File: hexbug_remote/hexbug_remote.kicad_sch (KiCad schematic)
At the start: 34 parts, among them J1 USB_C_Receptacle_USB2.0_16P, J2 Conn_01x02, J3 Conn_01x06, SW1 SW_Push, SW2 SW_Push, SW3 SW_Push, SW4 SW_Push, SW5 SW_Push, SW6 SW_Push, SW7 SW_SP4T_6PIN, SW8 SW_SPDT_3PIN, U1 TLV70033_SOT23-5, U2 MSPM01304xDGS20, U3 BQ21040DBV

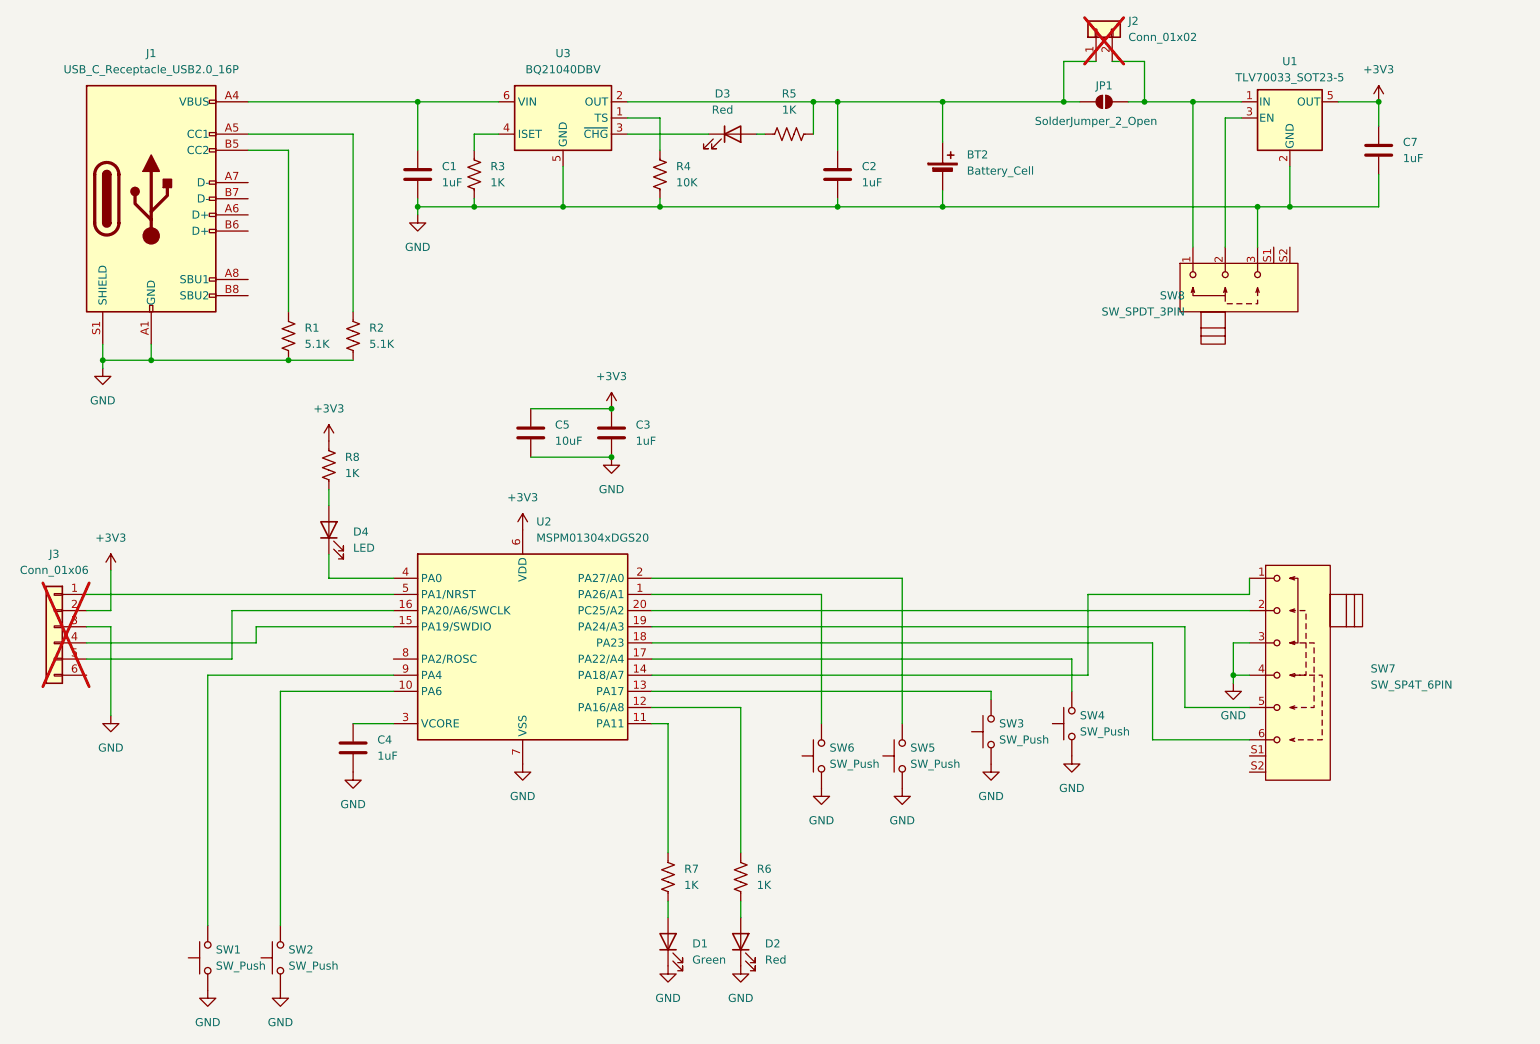
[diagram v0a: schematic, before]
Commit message: Update to use local db lib
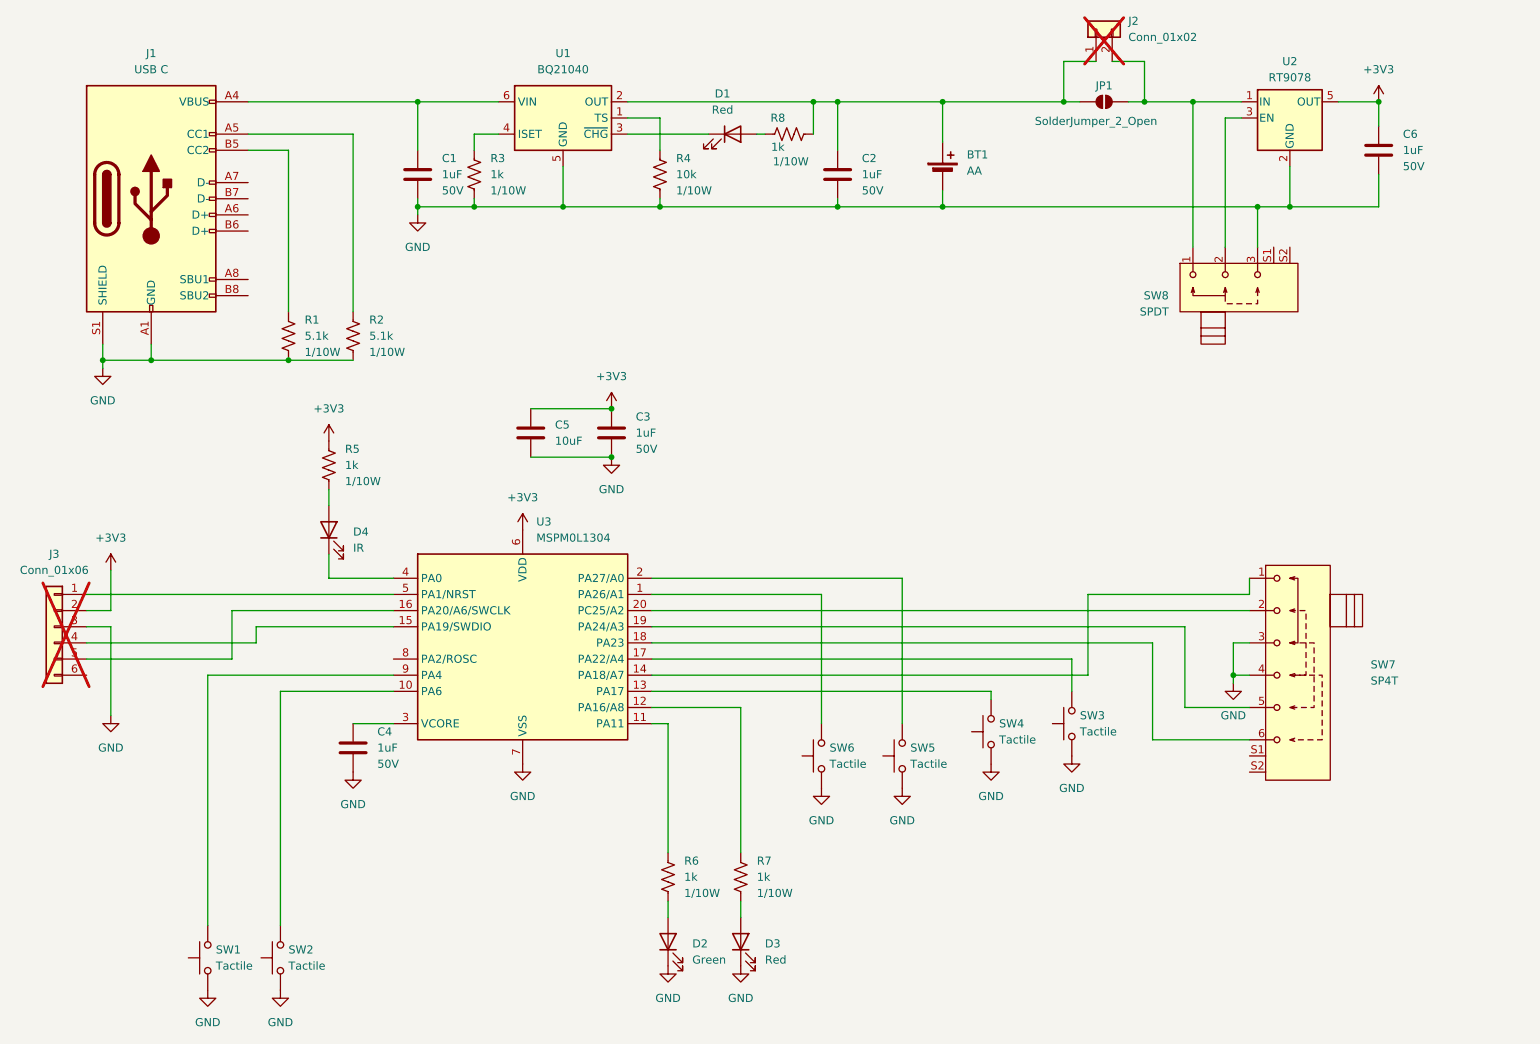
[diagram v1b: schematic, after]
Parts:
- removed BT2: Battery_Cell, Button_Samesky:Battery_Holder_MPD_BCAAPC, symbol Device:Battery_Cell
- removed C1, C2, C3, C4, C7: 1uF, Capacitor_SMD:C_0603_1608Metric_Pad1.08x0.95mm_HandSolder, symbol Device:C
- removed D1: Green, LED_SMD:LED_0603_1608Metric_Pad1.05x0.95mm_HandSolder, symbol Device:LED
- removed D2, D3: Red, LED_SMD:LED_0603_1608Metric_Pad1.05x0.95mm_HandSolder, symbol Device:LED
- removed D4: LED, LED_THT:LED_D5.0mm_Horizontal_O6.35mm_Z3.0mm, symbol Device:LED
- removed J1: USB_C_Receptacle_USB2.0_16P, Button_Samesky:USBC_16P, symbol Connector:USB_C_Receptacle_USB2.0_16P
- removed R1, R2: 5.1K, Resistor_SMD:R_0603_1608Metric_Pad0.98x0.95mm_HandSolder, symbol Device:R_US
- removed R3, R5, R6, R7, R8: 1K, Resistor_SMD:R_0603_1608Metric_Pad0.98x0.95mm_HandSolder, symbol Device:R_US
- removed R4: 10K, Resistor_SMD:R_0603_1608Metric_Pad0.98x0.95mm_HandSolder, symbol Device:R_US
- removed SW1, SW2: SW_Push, Button_Switch_THT:SW_Tactile_SPST_Angled_PTS645Vx58-2LFS, symbol Switch:SW_Push
- removed SW3, SW4, SW5, SW6: SW_Push, Button_Switch_THT:SW_TH_Tactile_Omron_B3F-106x, symbol Switch:SW_Push
- removed SW7: SW_SP4T_6PIN, Button_Samesky:SW_SPDT_Slide_Samesky_SLW-147844, symbol MCU_Local:SW_SP4T_6PIN
- removed SW8: SW_SPDT_3PIN, Button_Samesky:SW_SPDT_Slide_Samesky_SLW-129956, symbol MCU_Local:SW_SPDT_3PIN
- removed U1: TLV70033_SOT23-5, Package_TO_SOT_SMD:SOT-23-5, symbol Regulator_Linear:TLV70033_SOT23-5
- removed U2: MSPM01304xDGS20, Button_Samesky:TI_DGS20, symbol MCU_Local:MSPM0L1304xDGS20
- removed U3: BQ21040DBV, Package_TO_SOT_SMD:SOT-23-6, symbol Battery_Management:BQ21040DBV
- added BT1: AA, Local_Footprints:Battery_Holder_MPD_BCAAPC, symbol -Local_Lib:Mechanical/MECH-000005
- added C1, C2, C3, C4, C6: 1uF, Capacitor_SMD:C_0603_1608Metric, symbol -Local_Lib:Capacitors/CAP-000001
- added D1, D3: Red, LED_SMD:LED_0603_1608Metric_Pad1.05x0.95mm_HandSolder, symbol -Local_Lib:Diodes/DIO-000001
- added D2: Green, LED_SMD:LED_0603_1608Metric_Pad1.05x0.95mm_HandSolder, symbol -Local_Lib:Diodes/DIO-000002
- added D4: IR, LED_THT:LED_D5.0mm_Horizontal_O6.35mm_Z3.0mm, symbol -Local_Lib:Diodes/DIO-000003
- added J1: USB C, Local_Footprints:USBC_16P, symbol -Local_Lib:Connectors/CON-000001
- added R1, R2: 5.1k, Resistor_SMD:R_0603_1608Metric_Pad0.98x0.95mm_HandSolder, symbol -Local_Lib:Resistors/RES-000008
- added R3, R5, R6, R7, R8: 1k, Resistor_SMD:R_0603_1608Metric_Pad0.98x0.95mm_HandSolder, symbol -Local_Lib:Resistors/RES-000005
- added R4: 10k, Resistor_SMD:R_0603_1608Metric_Pad0.98x0.95mm_HandSolder, symbol -Local_Lib:Resistors/RES-000010
- added SW1, SW2: Tactile, Button_Switch_THT:SW_Tactile_SPST_Angled_PTS645Vx58-2LFS, symbol -Local_Lib:Mechanical/MECH-000004
- added SW3, SW4, SW5, SW6: Tactile, Button_Switch_THT:SW_TH_Tactile_Omron_B3F-106x, symbol -Local_Lib:Mechanical/MECH-000003
- added SW7: SP4T, Local_Footprints:SW_SP4T_Slide_Samesky_SLW-147844, symbol -Local_Lib:Mechanical/MECH-000002
- added SW8: SPDT, Local_Footprints:SW_SPDT_Slide_CK_SK12D07VG4, symbol -Local_Lib:Mechanical/MECH-000001
- added U1: BQ21040, Package_TO_SOT_SMD:SOT-23-6, symbol -Local_Lib:Integrated Circuits/IC-000001
- added U2: RT9078, Package_TO_SOT_SMD:SOT-23-5, symbol -Local_Lib:Integrated Circuits/IC-000003
- added U3: MSPM0L1304, Local_Footprints:TI_DGS20, symbol -Local_Lib:Integrated Circuits/IC-000002
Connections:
- net +3V3: now also C3.1, C6.1, R5.1, U2.5 (OUT), U3.6 (VDD)
- net GND: now also BT1.2 (-), C1.2, C2.2, C3.2, C4.2, C6.2, D2.1 (K), D3.1 (K), J1.A1 (GND), J1.A12 (GND), J1.B1 (GND), J1.B12 (GND), J1.S1 (SHIELD), R1.2, R2.2, R3.2, R4.2, SW1.1, SW2.1, SW3.1, SW4.1, SW5.1, SW6.1, SW7.3, SW7.4, SW8.3, U1.5 (GND), U2.2 (GND), U3.7 (VSS)
- net at J2.1 (Pin_1), JP1.1 (A): now also BT1.1 (+), C2.1, R8.1, U1.2 (OUT)
- net at J2.2 (Pin_2), JP1.2 (B): now also SW8.1, U2.1 (IN)
- net at J3.4 (Pin_4): now also U3.15 (PA19/SWDIO)
- net at J3.5 (Pin_5): now also U3.16 (PA20/A6/SWCLK)
- net at J3.1 (Pin_1): now also U3.5 (PA1/NRST)
- new net: D4.1 (K), U3.4 (PA0)
- new net: D4.2 (A), R5.2
- new net: C1.1, J1.A4 (VBUS), J1.A9 (VBUS), J1.B4 (VBUS), J1.B9 (VBUS), U1.6 (VIN)
- new net: SW2.2, U3.10 (PA6)
- new net: R3.1, U1.4 (ISET)
- new net: J1.A5 (CC1), R2.1
- new net: J1.B5 (CC2), R1.1
- new net: R7.1, U3.12 (PA16/A8)
- new net: D3.2 (A), R7.2
- new net: R6.1, U3.11 (PA11)
- new net: D2.2 (A), R6.2
- new net: SW5.2, U3.2 (PA27/A0)
- new net: SW4.2, U3.13 (PA17)
- new net: SW1.2, U3.9 (PA4)
- new net: D1.1 (K), U1.3 (~{CHG})
- new net: D1.2 (A), R8.2
- new net: SW8.2, U2.3 (EN)
- new net: SW6.2, U3.1 (PA26/A1)
- new net: SW7.1, U3.14 (PA18/A7)
- new net: SW3.2, U3.17 (PA22/A4)
- new net: SW7.6, U3.18 (PA23)
- new net: SW7.5, U3.19 (PA24/A3)
- new net: SW7.2, U3.20 (PC25/A2)
- new net: C4.1, U3.3 (VCORE)
- new net: R4.1, U1.1 (TS)

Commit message: Update Libraries
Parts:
- removed C5: 10uF, Capacitor_SMD:C_0603_1608Metric_Pad1.08x0.95mm_HandSolder, symbol Device:C
- added C5: 10uF, Capacitor_SMD:C_0603_1608Metric, symbol -Local_Lib:Capacitors/CAP-000005
- C1, C2, C3, C4, C6, D1, D2, D3: Package (none) -> 0603
- D4: Package (none) -> 5mm
- J1: Current (none) -> 5A; Other (none) -> 16 Pin; Package (none) -> USBC_16PIN
- R1, R2: LCSC Part Number - -> C23186; Manufacturer Part Number 1 RC0603FR-073K32L -> RC0603FR-075K1L; Manufacturer Part Number 2 - -> 0603WAF5101T5E; Package (none) -> 0603
- R3, R5, R6, R7, R8: LCSC Part Number - -> C21190; Manufacturer Part Number 2 - -> 0603WAF1001T5E; Package (none) -> 0603
- R4: LCSC Part Number C98220 -> C25804; Manufacturer Part Number 2 - -> 0603WAF1002T5E; Package (none) -> 0603
- SW1, SW2: Package (none) -> SW_6x6MM_4PIN_RA
- SW3, SW4, SW5, SW6: Package (none) -> SW_6x6MM_4PIN
- SW7: Package (none) -> SW_SP4T_6PIN_P2MM_RA
- SW8: Package (none) -> SW_SPDT_3PIN_P2MM_RA
- U1: Package (none) -> SOT-23-6
- U2: Package (none) -> TSOT-23-5
- U3: Package (none) -> VSSOP-20
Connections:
- net +3V3: now also C5.1
- net GND: now also C5.2

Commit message: --Add Gerber Files
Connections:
- net at R7.1: now also U3.11 (PA11); no longer U3.12 (PA16/A8)
- net at R6.1: now also U3.12 (PA16/A8); no longer U3.11 (PA11)
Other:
- moved on the sheet: D2, D3, R6, R7
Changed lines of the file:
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@@
 	(symbol
 		(lib_id "-Local_Lib:Resistors/RES-000005")
-		(at 139.7 165.1 0)
+		(at 128.27 165.1 0)
 		(unit 1)
 		(exclude_from_sim no)
@@
 		(fields_autoplaced yes)
 		(property "Reference" "R7"
-			(at 142.24 162.5599 0)
+			(at 130.81 162.5599 0)
 			(effects
 				(font
@@
 		)
 		(property "Value" "1k"
-			(at 142.24 165.0999 0)
+			(at 130.81 165.0999 0)
 			(effects
 				(font
@@
 		)
 		(property "Footprint" "Resistor_SMD:R_0603_1608Metric_Pad0.98x0.95mm_HandSolder"
-			(at 140.716 165.354 90)
+			(at 129.286 165.354 90)
 			(effects
 				(font
@@
 		)
 		(property "Datasheet" "~"
-			(at 139.7 165.1 0)
+			(at 128.27 165.1 0)
 			(effects
 				(font
@@
 		)
 		(property "Description" "Res Thick 1k 1/10W 1% 0603"
-			(at 139.7 165.1 0)
+			(at 128.27 165.1 0)
 			(effects
 				(font
@@
 		)
 		(property "Power" "1/10W"
-			(at 142.24 167.6399 0)
+			(at 130.81 167.6399 0)
 			(effects
 				(font
@@
 		)
 		(property "Tolerance" "1%"
-			(at 139.7 165.1 0)
+			(at 128.27 165.1 0)
 			(effects
 				(font
@@
 		)
 		(property "Manufacturer" "Yageo"
-			(at 139.7 165.1 0)
+			(at 128.27 165.1 0)
 			(effects
 				(font
@@
 		)
 		(property "Manufacturer Part Number 1" "RC0603FR-071KL"
-			(at 139.7 165.1 0)
+			(at 128.27 165.1 0)
 			(effects
 				(font
@@
 		)
 		(property "Manufacturer 2" "Uni-Royal"
-			(at 139.7 165.1 0)
+			(at 128.27 165.1 0)
 			(effects
 				(font
@@
 		)
 		(property "Manufacturer Part Number 2" "0603WAF1001T5E"
-			(at 139.7 165.1 0)
+			(at 128.27 165.1 0)
 			(effects
 				(font
@@
 		)
 		(property "LCSC Part Number" "C21190"
-			(at 139.7 165.1 0)
+			(at 128.27 165.1 0)
 			(effects
 				(font
@@
 		)
 		(property "Package" "0603"
-			(at 139.7 165.1 0)
+			(at 128.27 165.1 0)
 			(effects
 				(font
@@
 	(symbol
 		(lib_id "-Local_Lib:Resistors/RES-000005")
-		(at 128.27 165.1 0)
+		(at 139.7 165.1 0)
 		(unit 1)
 		(exclude_from_sim no)
@@
 		(fields_autoplaced yes)
 		(property "Reference" "R6"
-			(at 130.81 162.5599 0)
+			(at 142.24 162.5599 0)
 			(effects
 				(font
@@
 		)
 		(property "Value" "1k"
-			(at 130.81 165.0999 0)
+			(at 142.24 165.0999 0)
 			(effects
 				(font
@@
 		)
 		(property "Footprint" "Resistor_SMD:R_0603_1608Metric_Pad0.98x0.95mm_HandSolder"
-			(at 129.286 165.354 90)
+			(at 140.716 165.354 90)
 			(effects
 				(font
@@
 		)
 		(property "Datasheet" "~"
-			(at 128.27 165.1 0)
+			(at 139.7 165.1 0)
 			(effects
 				(font
@@
 		)
 		(property "Description" "Res Thick 1k 1/10W 1% 0603"
-			(at 128.27 165.1 0)
+			(at 139.7 165.1 0)
 			(effects
 				(font
@@
 		)
 		(property "Power" "1/10W"
-			(at 130.81 167.6399 0)
+			(at 142.24 167.6399 0)
 			(effects
 				(font
@@
 		)
 		(property "Tolerance" "1%"
-			(at 128.27 165.1 0)
+			(at 139.7 165.1 0)
 			(effects
 				(font
@@
 		)
 		(property "Manufacturer" "Yageo"
-			(at 128.27 165.1 0)
+			(at 139.7 165.1 0)
 			(effects
 				(font
@@
 		)
 		(property "Manufacturer Part Number 1" "RC0603FR-071KL"
-			(at 128.27 165.1 0)
+			(at 139.7 165.1 0)
 			(effects
 				(font
@@
 		)
 		(property "Manufacturer 2" "Uni-Royal"
-			(at 128.27 165.1 0)
+			(at 139.7 165.1 0)
 			(effects
 				(font
@@
 		)
 		(property "Manufacturer Part Number 2" "0603WAF1001T5E"
-			(at 128.27 165.1 0)
+			(at 139.7 165.1 0)
 			(effects
 				(font
@@
 		)
 		(property "LCSC Part Number" "C21190"
-			(at 128.27 165.1 0)
+			(at 139.7 165.1 0)
 			(effects
 				(font
@@
 		)
 		(property "Package" "0603"
-			(at 128.27 165.1 0)
+			(at 139.7 165.1 0)
 			(effects
 				(font
@@
 	(symbol
 		(lib_id "-Local_Lib:Diodes/DIO-000002")
-		(at 128.27 175.26 90)
+		(at 139.7 175.26 90)
 		(unit 1)
 		(exclude_from_sim no)
@@
 		(fields_autoplaced yes)
 		(property "Reference" "D2"
-			(at 132.08 175.5774 90)
+			(at 143.51 175.5774 90)
 			(effects
 				(font
@@
 		)
 		(property "Value" "Green"
-			(at 132.08 178.1174 90)
+			(at 143.51 178.1174 90)
 			(effects
 				(font
@@
 		)
 		(property "Footprint" "LED_SMD:LED_0603_1608Metric_Pad1.05x0.95mm_HandSolder"
-			(at 128.27 175.26 0)
+			(at 139.7 175.26 0)
 			(effects
 				(font
@@
 		)
 		(property "Datasheet" "~"
-			(at 128.27 175.26 0)
+			(at 139.7 175.26 0)
 			(effects
 				(font
@@
 		)
 		(property "Description" "Dio LED Green 2.7V 20mA 520nm 0603"
-			(at 128.27 175.26 0)
+			(at 139.7 175.26 0)
 			(effects
 				(font
@@
 		)
 		(property "Sim.Pins" "1=K 2=A"
-			(at 128.27 175.26 0)
+			(at 139.7 175.26 0)
 			(effects
 				(font
@@
 		)
 		(property "Type" "LED"
-			(at 128.27 175.26 0)
+			(at 139.7 175.26 0)
 			(effects
 				(font
@@
 		)
 		(property "VF" "2.7V"
-			(at 128.27 175.26 0)
+			(at 139.7 175.26 0)
 			(effects
 				(font
@@
 		)
 		(property "Current" "20mA"
-			(at 128.27 175.26 0)
+			(at 139.7 175.26 0)
 			(effects
 				(font
@@
 		)
 		(property "VR" "-"
-			(at 128.27 175.26 0)
+			(at 139.7 175.26 0)
 			(effects
 				(font
@@
 		)
 		(property "trr" "-"
-			(at 128.27 175.26 0)
+			(at 139.7 175.26 0)
 			(effects
 				(font
@@
 		)
 		(property "other" "520nm"
-			(at 128.27 175.26 0)
+			(at 139.7 175.26 0)
 			(effects
 				(font
@@
 		)
 		(property "Manufacturer" "Hubei KENTO Elec"
-			(at 128.27 175.26 0)
+			(at 139.7 175.26 0)
 			(effects
 				(font
@@
 		)
 		(property "Manufacturer Part Number 1" "KT-0603G"
-			(at 128.27 175.26 0)
+			(at 139.7 175.26 0)
 			(effects
 				(font
@@
 		)
 		(property "Manufacturer 2" "Lite-On"
-			(at 128.27 175.26 0)
+			(at 139.7 175.26 0)
 			(effects
 				(font
@@
 		)
 		(property "Manufacturer Part Number 2" "LTST-C193TGKT-5A"
-			(at 128.27 175.26 0)
+			(at 139.7 175.26 0)
 			(effects
 				(font
@@
 		)
 		(property "LCSC Part Number" "C12624"
-			(at 128.27 175.26 0)
+			(at 139.7 175.26 0)
 			(effects
 				(font
@@
 		)
 		(property "Package" "0603"
-			(at 128.27 175.26 0)
+			(at 139.7 175.26 0)
 			(effects
 				(font
@@
 		)
 		(instances
-			(project ""
+			(project "hexbug_remote"
 				(path "/04383375-1719-4c0d-877c-ff4fedd005c5"
 					(reference "D2")
@@
 	(symbol
 		(lib_id "-Local_Lib:Diodes/DIO-000001")
-		(at 139.7 175.26 90)
+		(at 128.27 175.26 90)
 		(unit 1)
 		(exclude_from_sim no)
@@
 		(fields_autoplaced yes)
 		(property "Reference" "D3"
-			(at 143.51 175.5774 90)
+			(at 132.08 175.5774 90)
 			(effects
 				(font
@@
 		)
 		(property "Value" "Red"
-			(at 143.51 178.1174 90)
+			(at 132.08 178.1174 90)
 			(effects
 				(font
@@
 		)
 		(property "Footprint" "LED_SMD:LED_0603_1608Metric_Pad1.05x0.95mm_HandSolder"
-			(at 139.7 175.26 0)
+			(at 128.27 175.26 0)
 			(effects
 				(font
@@
 		)
 		(property "Datasheet" "~"
-			(at 139.7 175.26 0)
+			(at 128.27 175.26 0)
 			(effects
 				(font
@@
 		)
 		(property "Description" "Dio LED Red 2V 20mA 620nm 0603"
-			(at 139.7 175.26 0)
+			(at 128.27 175.26 0)
 			(effects
 				(font
@@
 		)
 		(property "Sim.Pins" "1=K 2=A"
-			(at 139.7 175.26 0)
+			(at 128.27 175.26 0)
 			(effects
 				(font
@@
 		)
 		(property "Type" "LED"
-			(at 139.7 175.26 0)
+			(at 128.27 175.26 0)
 			(effects
 				(font
@@
 		)
 		(property "VF" "2V"
-			(at 139.7 175.26 0)
+			(at 128.27 175.26 0)
 			(effects
 				(font
@@
 		)
 		(property "Current" "20mA"
-			(at 139.7 175.26 0)
+			(at 128.27 175.26 0)
 			(effects
 				(font
@@
 		)
 		(property "VR" "-"
-			(at 139.7 175.26 0)
+			(at 128.27 175.26 0)
 			(effects
 				(font
@@
 		)
 		(property "trr" "-"
-			(at 139.7 175.26 0)
+			(at 128.27 175.26 0)
 			(effects
 				(font
@@
 		)
 		(property "other" "620nm"
-			(at 139.7 175.26 0)
+			(at 128.27 175.26 0)
 			(effects
 				(font
@@
 		)
 		(property "Manufacturer" "Hubei KENTO Elec"
-			(at 139.7 175.26 0)
+			(at 128.27 175.26 0)
 			(effects
 				(font
@@
 		)
 		(property "Manufacturer Part Number 1" "KT-0603R"
-			(at 139.7 175.26 0)
+			(at 128.27 175.26 0)
 			(effects
 				(font
@@
 		)
 		(property "Manufacturer 2" "Lite-On"
-			(at 139.7 175.26 0)
+			(at 128.27 175.26 0)
 			(effects
 				(font
@@
 		)
 		(property "Manufacturer Part Number 2" "LTST-C190EKT"
-			(at 139.7 175.26 0)
+			(at 128.27 175.26 0)
 			(effects
 				(font
@@
 		)
 		(property "LCSC Part Number" "C2286"
-			(at 139.7 175.26 0)
+			(at 128.27 175.26 0)
 			(effects
 				(font
@@
 		)
 		(property "Package" "0603"
-			(at 139.7 175.26 0)
+			(at 128.27 175.26 0)
 			(effects
 				(font
@@
 		)
 		(instances
-			(project ""
+			(project "hexbug_remote"
 				(path "/04383375-1719-4c0d-877c-ff4fedd005c5"
 					(reference "D3")
